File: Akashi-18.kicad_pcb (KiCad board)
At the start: 2 copper layers, 54.6 x 91.4 mm, 13 parts, among them Q1 DTC143Z, Q2 DTC143Z, Q3 DTC143Z, SW1 B3FS, SW2 B3FS, SW3 B3FS, U1 Pico

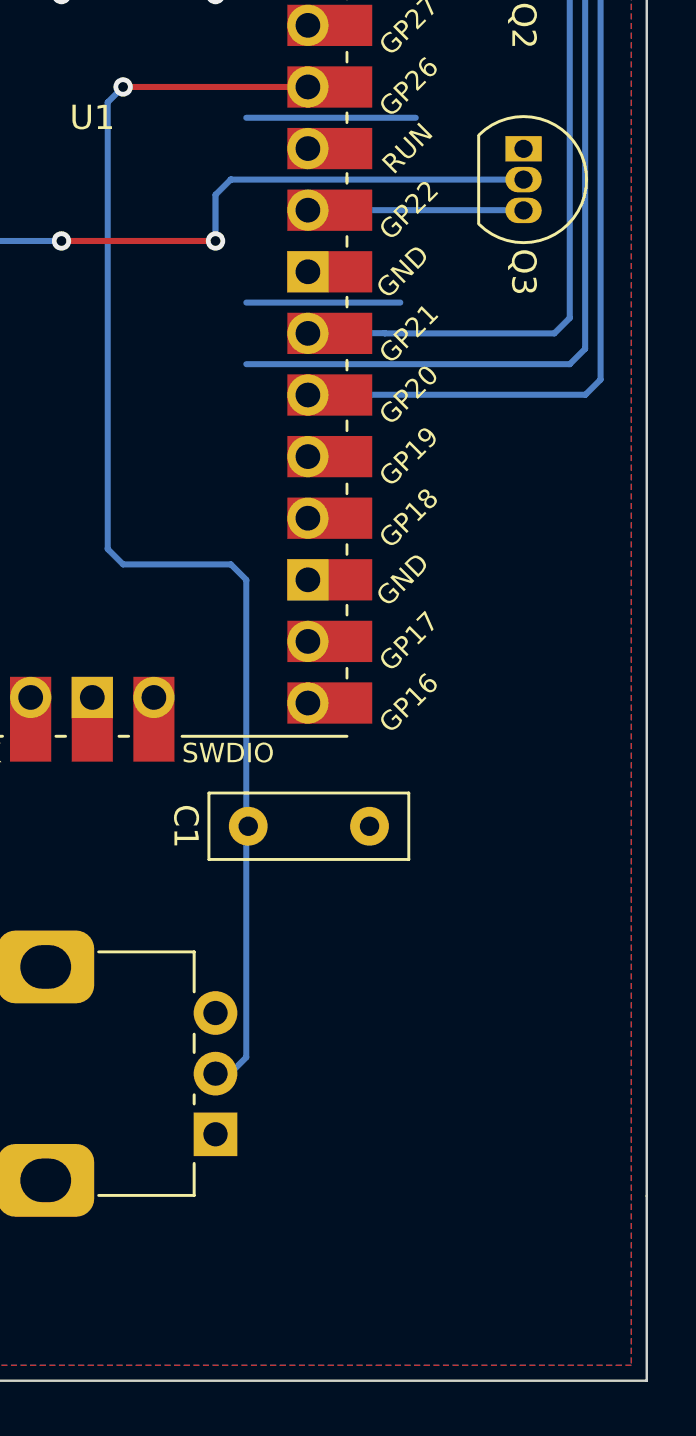
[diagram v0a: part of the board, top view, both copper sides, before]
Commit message: Add reset switch.
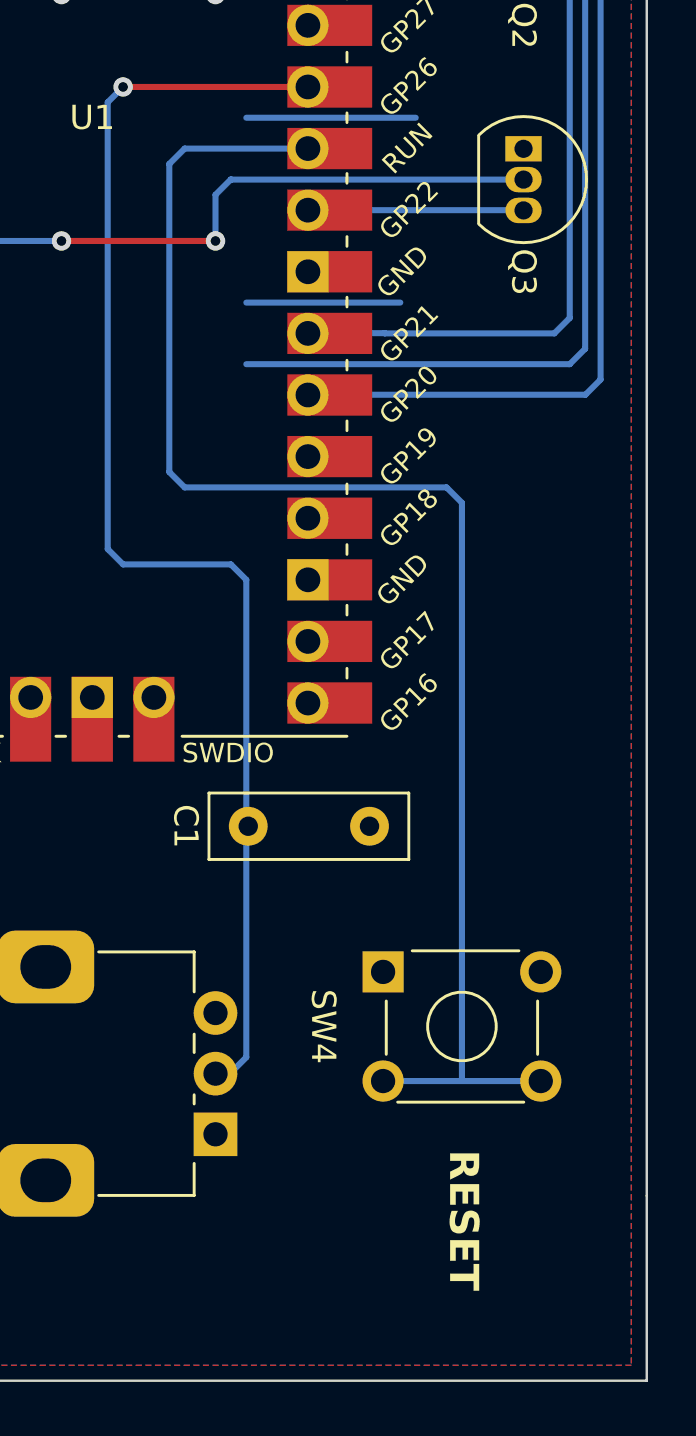
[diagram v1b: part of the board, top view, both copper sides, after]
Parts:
- added SW4: B3FS, Button_Switch_THT:SW_TH_Tactile_Omron_B3F-10xx, F.Cu at (132.6, 125.4)
- R1: value 150 -> 1.5k
- R2: value 240 -> 2.7k
- R3: value 91 -> 1k
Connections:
- U1 pad 30: unconnected-(U1-RUN-Pad30) -> /RESET
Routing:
- net /RESET: track 0.00 -> 61.6 mm
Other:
- board text added: "RESET"
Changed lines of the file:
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@@
   (net 31 "unconnected-(U1-GPIO4-Pad6)")
   (net 32 "unconnected-(U1-GPIO10-Pad14)")
-  (net 33 "unconnected-(U1-RUN-Pad30)")
+  (net 33 "/RESET")
   (net 34 "unconnected-(U1-GPIO27_ADC1-Pad32)")
   (net 35 "unconnected-(U1-GPIO28_ADC2-Pad34)")
@@
         (effects (font (size 1 1) (thickness 0.15)))
     )
-    (fp_text value "150" (at 5.08 2.37 90) (layer "F.Fab")
+    (fp_text value "1.5k" (at 5.08 2.37 90) (layer "F.Fab")
         (effects (font (size 1 1) (thickness 0.15)))
     )
@@
         (effects (font (size 1 1) (thickness 0.15)))
     )
-    (fp_text value "91" (at 5.08 2.37 90) (layer "F.Fab")
+    (fp_text value "1k" (at 5.08 2.37 90) (layer "F.Fab")
         (effects (font (size 1 1) (thickness 0.15)))
     )
@@
     )
   )
+  (footprint "Button_Switch_THT:SW_TH_Tactile_Omron_B3F-10xx" (layer "F.Cu")
+    (at 132.64 125.385)
+    (descr "SW_TH_Tactile_Omron_B3F-10xx_https://www.omron.com/ecb/products/pdf/en-b3f.pdf")
+    (tags "Omron B3F-10xx")
+    (property "Sheetfile" "Akashi-18.kicad_sch")
+    (property "Sheetname" "")
+    (property "ki_description" "Omron B3FS 6x6mm single pole normally-open tactile switch")
+    (property "ki_keywords" "switch normally-open pushbutton push-button")
+    (attr through_hole)
+    (fp_text reference "SW4" (at -2.465 2.25 -90 unlocked) (layer "F.SilkS")
+        (effects (font (size 1 1) (thickness 0.15)))
+    )
+    (fp_text value "B3FS" (at 3.2 6.5) (layer "F.Fab")
+        (effects (font (size 1 1) (thickness 0.15)))
+    )
+    (fp_text user "${REFERENCE}" (at 3.25 2.25) (layer "F.Fab")
+        (effects (font (size 1 1) (thickness 0.15)))
+    )
+    (fp_line (start 0.13 3.4) (end 0.13 1.2)
+      (stroke (width 0.12) (type solid)) (layer "F.SilkS"))
+    (fp_line (start 0.6 5.37) (end 5.8 5.37)
+      (stroke (width 0.12) (type solid)) (layer "F.SilkS"))
+    (fp_line (start 1.2 -0.87) (end 5.6 -0.87)
+      (stroke (width 0.12) (type solid)) (layer "F.SilkS"))
+    (fp_line (start 6.37 1.2) (end 6.37 3.4)
+      (stroke (width 0.12) (type solid)) (layer "F.SilkS"))
+    (fp_circle (center 3.25 2.25) (end 4.25 3.25)
+      (stroke (width 0.12) (type solid)) (fill none) (layer "F.SilkS"))
+    (fp_line (start -1.1 -1.1) (end -1.1 5.6)
+      (stroke (width 0.05) (type solid)) (layer "F.CrtYd"))
+    (fp_line (start -1.1 -1.1) (end 7.6 -1.1)
+      (stroke (width 0.05) (type solid)) (layer "F.CrtYd"))
+    (fp_line (start -1.1 5.6) (end 7.6 5.6)
+      (stroke (width 0.05) (type solid)) (layer "F.CrtYd"))
+    (fp_line (start 7.6 5.6) (end 7.6 -1.1)
+      (stroke (width 0.05) (type solid)) (layer "F.CrtYd"))
+    (fp_line (start 0.25 -0.75) (end 0.25 5.25)
+      (stroke (width 0.1) (type solid)) (layer "F.Fab"))
+    (fp_line (start 0.25 -0.75) (end 6.25 -0.75)
+      (stroke (width 0.1) (type solid)) (layer "F.Fab"))
+    (fp_line (start 0.25 5.25) (end 6.25 5.25)
+      (stroke (width 0.1) (type solid)) (layer "F.Fab"))
+    (fp_line (start 6.25 -0.75) (end 6.25 5.25)
+      (stroke (width 0.1) (type solid)) (layer "F.Fab"))
+    (pad "1" thru_hole rect (at 0 0) (size 1.7 1.7) (drill 1) (layers "*.Cu" "*.Mask")
+      (net 5 "GND") (pinfunction "1") (pintype "passive"))
+    (pad "1" thru_hole circle (at 6.5 0) (size 1.7 1.7) (drill 1) (layers "*.Cu" "*.Mask")
+      (net 5 "GND") (pinfunction "1") (pintype "passive"))
+    (pad "2" thru_hole circle (at 0 4.5) (size 1.7 1.7) (drill 1) (layers "*.Cu" "*.Mask")
+      (net 33 "/RESET") (pinfunction "2") (pintype "passive"))
+    (pad "2" thru_hole circle (at 6.5 4.5) (size 1.7 1.7) (drill 1) (layers "*.Cu" "*.Mask")
+      (net 33 "/RESET") (pinfunction "2") (pintype "passive"))
+    (model "${KICAD6_3DMODEL_DIR}/Button_Switch_THT.3dshapes/SW_TH_Tactile_Omron_B3F-10xx.wrl"
+      (offset (xyz 0 0 0))
+      (scale (xyz 1 1 1))
+      (rotate (xyz 0 0 0))
+    )
+  )
   (footprint "Resistor_THT:R_Axial_DIN0207_L6.3mm_D2.5mm_P10.16mm_Horizontal" (layer "F.Cu")
     (at 99.06 73.66 -90)
@@
         (effects (font (size 1 1) (thickness 0.15)))
     )
-    (fp_text value "240" (at 5.08 2.37 90) (layer "F.Fab")
+    (fp_text value "2.7k" (at 5.08 2.37 90) (layer "F.Fab")
         (effects (font (size 1 1) (thickness 0.15)))
     )
@@
       (net 11 "/BLUE") (pinfunction "GPIO22") (pintype "bidirectional"))
     (pad "30" thru_hole oval (at 8.89 1.27) (size 1.7 1.7) (drill 1.02) (layers "*.Cu" "*.Mask")
-      (net 33 "unconnected-(U1-RUN-Pad30)") (pinfunction "RUN") (pintype "input+no_connect"))
+      (net 33 "/RESET") (pinfunction "RUN") (pintype "input"))
     (pad "30" smd rect (at 8.89 1.27) (size 3.5 1.7) (drill (offset 0.9 0)) (layers "F.Cu" "F.Mask")
-      (net 33 "unconnected-(U1-RUN-Pad30)") (pinfunction "RUN") (pintype "input+no_connect"))
+      (net 33 "/RESET") (pinfunction "RUN") (pintype "input"))
     (pad "31" thru_hole oval (at 8.89 -1.27) (size 1.7 1.7) (drill 1.02) (layers "*.Cu" "*.Mask")
       (net 12 "Net-(U1-GPIO26_ADC0)") (pinfunction "GPIO26_ADC0") (pintype "bidirectional"))
@@
   )
   (gr_text "R : GP20\nG : GP21\nB : GP22" (at 105.41 53.975 270) (layer "F.SilkS")
+    (effects (font (size 1.2 1.2) (thickness 0.2) bold) (justify left bottom))
+  )
+  (gr_text "RESET" (at 135.255 132.715 270) (layer "F.SilkS")
     (effects (font (size 1.2 1.2) (thickness 0.2) bold) (justify left bottom))
   )
@@
   (segment (start 104.14 106.68) (end 104.775 106.045) (width 0.25) (layer "B.Cu") (net 15))
   (segment (start 96.2 106.68) (end 104.14 106.68) (width 0.25) (layer "B.Cu") (net 15))
+  (segment (start 135.89 129.885) (end 132.64 129.885) (width 0.25) (layer "B.Cu") (net 33))
+  (segment (start 123.825 92.075) (end 123.825 104.775) (width 0.25) (layer "B.Cu") (net 33))
+  (segment (start 123.825 104.775) (end 124.46 105.41) (width 0.25) (layer "B.Cu") (net 33))
+  (segment (start 135.89 106.045) (end 135.89 129.885) (width 0.25) (layer "B.Cu") (net 33))
+  (segment (start 139.14 129.885) (end 135.89 129.885) (width 0.25) (layer "B.Cu") (net 33))
+  (segment (start 135.255 105.41) (end 135.89 106.045) (width 0.25) (layer "B.Cu") (net 33))
+  (segment (start 124.46 91.44) (end 123.825 92.075) (width 0.25) (layer "B.Cu") (net 33))
+  (segment (start 124.46 105.41) (end 135.255 105.41) (width 0.25) (layer "B.Cu") (net 33))
+  (segment (start 129.54 91.44) (end 124.46 91.44) (width 0.25) (layer "B.Cu") (net 33))
   (segment (start 127 97.79) (end 133.35 97.79) (width 0.25) (layer "B.Cu") (net 42))
   (segment (start 127 90.17) (end 133.985 90.17) (width 0.25) (layer "B.Cu") (net 42))
